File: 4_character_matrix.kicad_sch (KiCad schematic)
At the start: 26 parts, among them U25 LSHD-5503, U26 LSHD-5503, U27 LSHD-5503, U28 LSHD-5503, U29 SN74LVC244A, U30 SN74LVC244A

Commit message: change in display module
- Created new sheets
- Reordered the sheets
- Created the footprint for the display
- 3D model of the display
- MCU selection
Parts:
- removed C18, C20: 10u, symbol Device:C
- removed U25, U26, U27, U28: LSHD-5503, symbol precision_clock:LSHD-5503
- added U22, U24, U25, U27: SC10-21SURKWA, precision_clock:SC10-21SURKWA, symbol precision_clock:SC10-21SURKWA
- U23: renamed from U29; footprint (none) -> Package_SO:TSSOP-20_4.4x6.5mm_P0.65mm
- U26: renamed from U30; footprint (none) -> Package_SO:TSSOP-20_4.4x6.5mm_P0.65mm
- renumbered C19 to C7, C21 to C8, D2 to D1, D3 to D2, D4 to D3, D5 to D4, R34 to R25, R35 to R26, R36 to R27, R37 to R28, R38 to R29, R39 to R30, R40 to R31, R41 to R32, R42 to R33, R43 to R34, R44 to R35, R45 to R36
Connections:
- net BA0: now also U22.7 (A), U24.7 (A), U25.7 (A), U27.7 (A)
- net BA1: now also U22.6 (B), U24.6 (B), U25.6 (B), U27.6 (B)
- net BA2: now also U22.4 (C), U24.4 (C), U25.4 (C), U27.4 (C)
- net BA3: now also U22.2 (D), U24.2 (D), U25.2 (D), U27.2 (D)
- net BA4: now also U22.1 (E), U24.1 (E), U25.1 (E), U27.1 (E)
- net BA5: now also U22.9 (F), U24.9 (F), U25.9 (F), U27.9 (F)
- net BA6: now also U22.10 (G), U24.10 (G), U25.10 (G), U27.10 (G)
- net BA7: now also U22.5 (DP), U24.5 (DP), U25.5 (DP), U27.5 (DP)
- net BK0: now also U22.3 (CC), U22.8 (CC)
- net BK1: now also U24.3 (CC), U24.8 (CC)
- net BK2: now also U25.3 (CC), U25.8 (CC)
- net BK3: now also U27.3 (CC), U27.8 (CC)

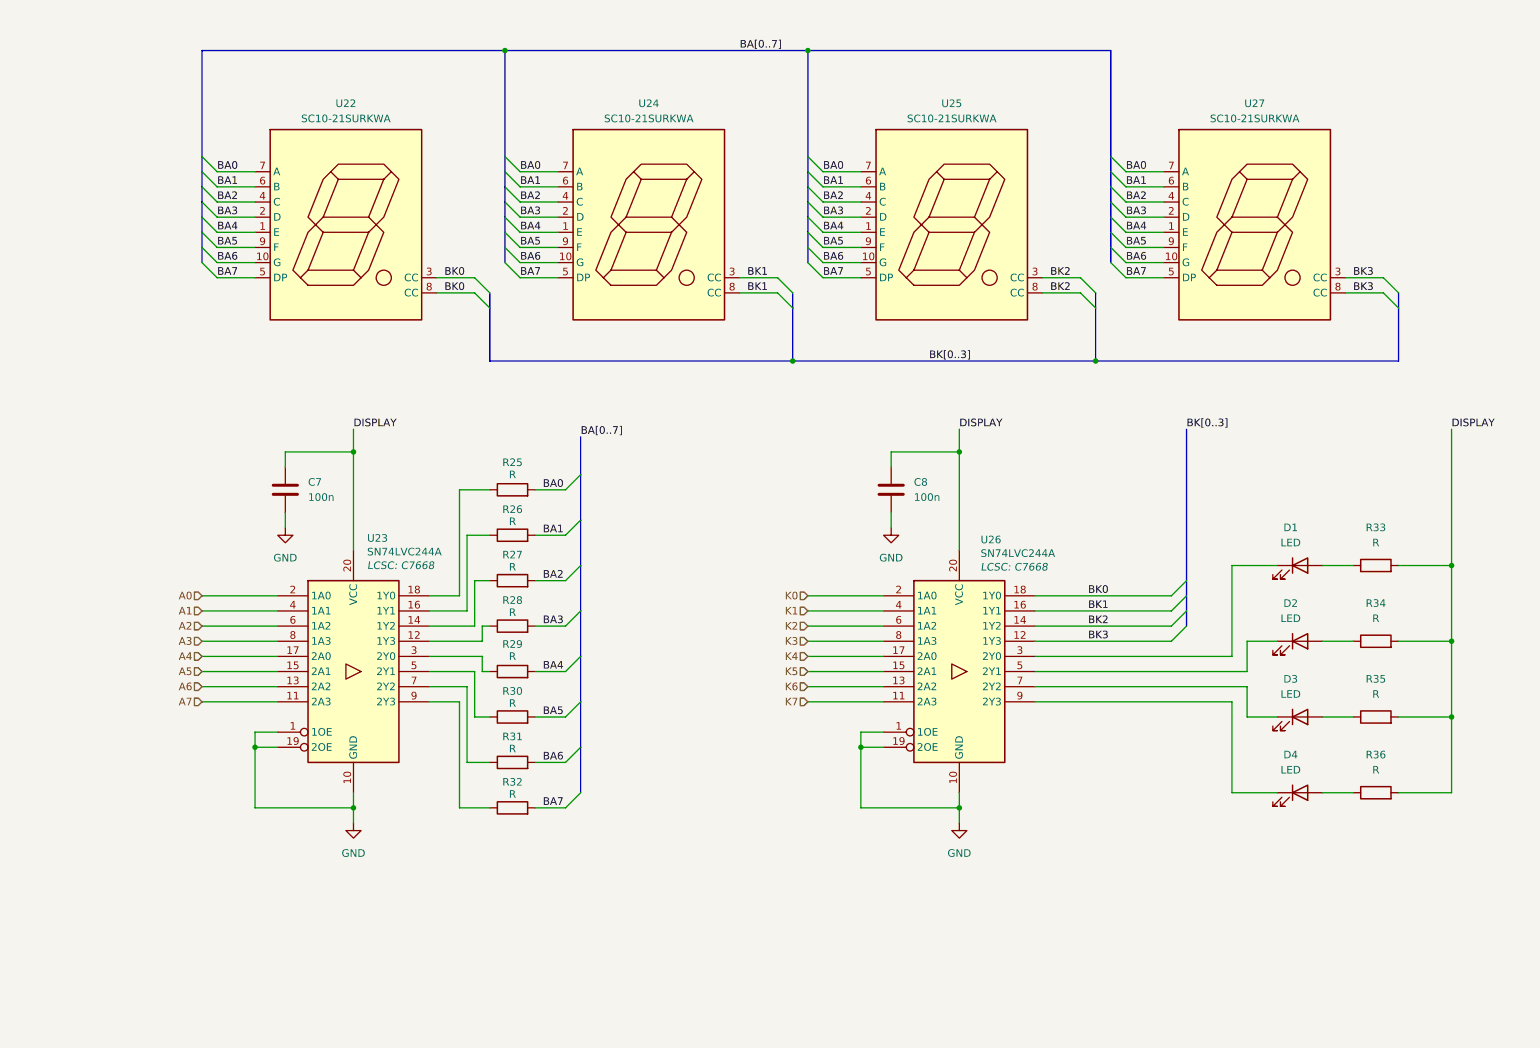
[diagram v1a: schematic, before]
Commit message: change in display module
- changes the display to a common anode type display
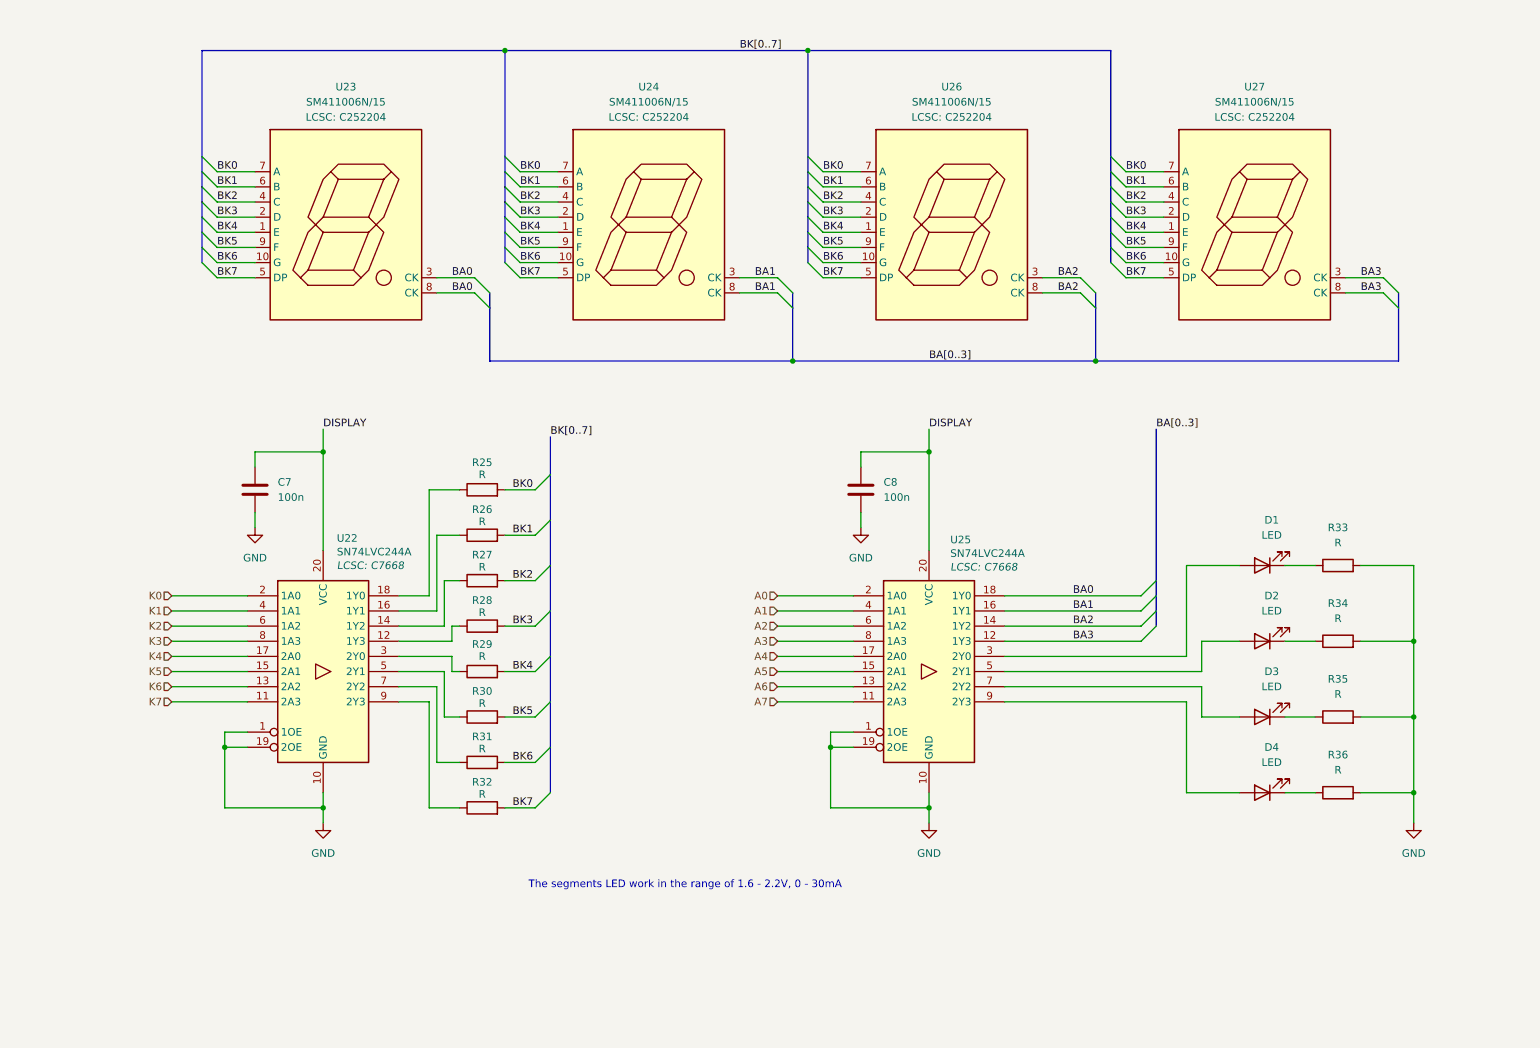
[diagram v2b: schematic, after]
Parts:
- removed U22, U24, U25, U27: SC10-21SURKWA, precision_clock:SC10-21SURKWA, symbol precision_clock:SC10-21SURKWA
- removed U23, U26: SN74LVC244A, Package_SO:TSSOP-20_4.4x6.5mm_P0.65mm, symbol 74xx:74AHC244
- added U22, U25: SN74LVC244A, Package_SO:TSSOP-20_4.4x6.5mm_P0.65mm, symbol 74xx:74AHC244
- added U23, U24, U26, U27: SM411006N/15, precision_clock:SM411006N15, symbol precision_clock:SM411006N/15
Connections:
- net A0: now also U25.2 (1A0)
- net A1: now also U25.4 (1A1)
- net A2: now also U25.6 (1A2)
- net A3: now also U25.8 (1A3)
- net A4: now also U25.17 (2A0)
- net A5: now also U25.15 (2A1)
- net A6: now also U25.13 (2A2)
- net A7: now also U25.11 (2A3)
- net BA0: now also U23.3 (CK), U23.8 (CK), U25.18 (1Y0); no longer R25.2
- net BA1: now also U24.3 (CK), U24.8 (CK), U25.16 (1Y1); no longer R26.2
- net BA2: now also U25.14 (1Y2), U26.3 (CK), U26.8 (CK); no longer R27.2
- net BA3: now also U25.12 (1Y3), U27.3 (CK), U27.8 (CK); no longer R28.2
- net BK0: now also R25.2, U23.7 (A), U24.7 (A), U26.7 (A), U27.7 (A)
- net BK1: now also R26.2, U23.6 (B), U24.6 (B), U26.6 (B), U27.6 (B)
- net BK2: now also R27.2, U23.4 (C), U24.4 (C), U26.4 (C), U27.4 (C)
- net BK3: now also R28.2, U23.2 (D), U24.2 (D), U26.2 (D), U27.2 (D)
- net DISPLAY: now also U22.20 (VCC), U25.20 (VCC); no longer R33.2, R34.2, R35.2, R36.2
- net GND: now also R33.2, R34.2, R35.2, R36.2, U22.1 (1OE), U22.10 (GND), U22.19 (2OE), U25.1 (1OE), U25.10 (GND), U25.19 (2OE)
- net K0: now also U22.2 (1A0)
- net K1: now also U22.4 (1A1)
- net K2: now also U22.6 (1A2)
- net K3: now also U22.8 (1A3)
- net K4: now also U22.17 (2A0)
- net K5: now also U22.15 (2A1)
- net K6: now also U22.13 (2A2)
- net K7: now also U22.11 (2A3)
- net at R32.1: now also U22.9 (2Y3)
- net at D1.1 (K): now also R33.1
- net at D1.2 (A): now also U25.3 (2Y0); no longer R33.1
- net at D2.1 (K): now also R34.1
- net at D3.1 (K): now also R35.1
- net at D4.1 (K): now also R36.1
- net at R29.1: now also U22.3 (2Y0)
- net at D2.2 (A): now also U25.5 (2Y1); no longer R34.1
- net at D3.2 (A): now also U25.7 (2Y2); no longer R35.1
- net at R26.1: now also U22.16 (1Y1)
- net at R30.1: now also U22.5 (2Y1)
- net at R28.1: now also U22.12 (1Y3)
- net at R27.1: now also U22.14 (1Y2)
- net at R25.1: now also U22.18 (1Y0)
- net at R31.1: now also U22.7 (2Y2)
- net at D4.2 (A): now also U25.9 (2Y3); no longer R36.1
- net BA4 renamed BK4
- net BK4: now also U23.1 (E), U24.1 (E), U26.1 (E), U27.1 (E)
- net BA5 renamed BK5
- net BK5: now also U23.9 (F), U24.9 (F), U26.9 (F), U27.9 (F)
- net BA6 renamed BK6
- net BK6: now also U23.10 (G), U24.10 (G), U26.10 (G), U27.10 (G)
- net BA7 renamed BK7
- net BK7: now also U23.5 (DP), U24.5 (DP), U26.5 (DP), U27.5 (DP)
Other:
- note added: "The segments LED work in the range of 1.6 - 2.2V, 0 - 30mA"

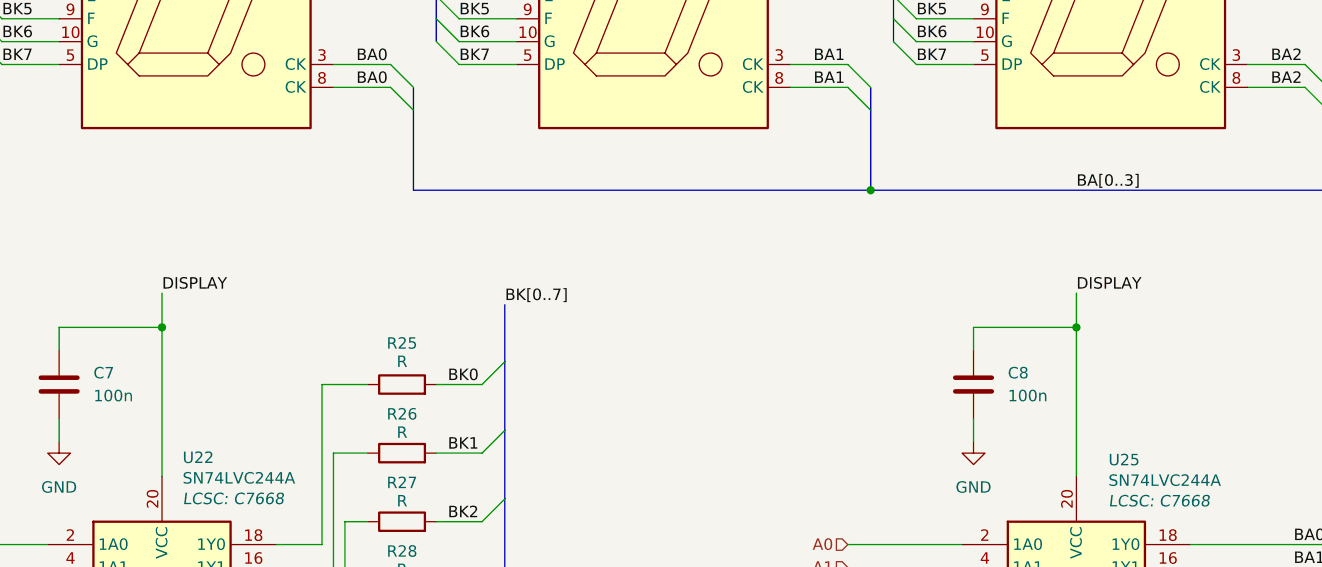
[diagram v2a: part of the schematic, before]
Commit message: primary MCU changes
- added preliminary decoupling
- added LSE
- added flash memory
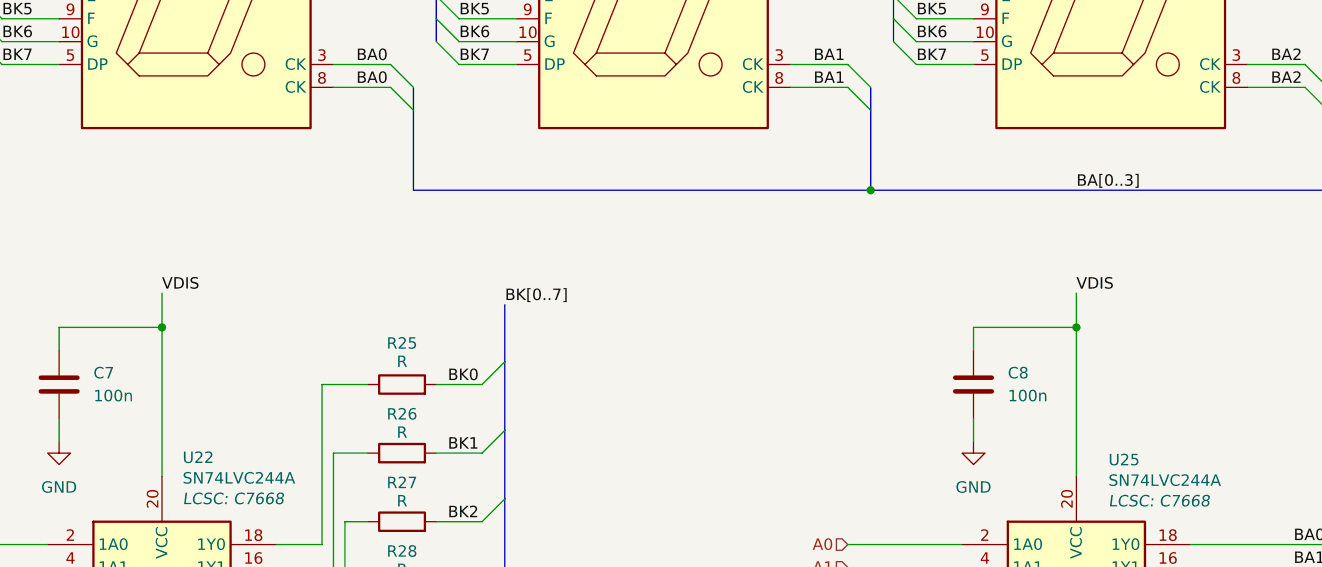
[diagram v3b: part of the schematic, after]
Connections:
- net DISPLAY renamed VDIS
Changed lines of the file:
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@@
 		)
 	)
-	(label "DISPLAY"
+	(label "VDIS"
 		(at 71.12 88.9 0)
 		(effects
@@
 		)
 	)
-	(label "DISPLAY"
+	(label "VDIS"
 		(at 172.72 88.9 0)
 		(effects

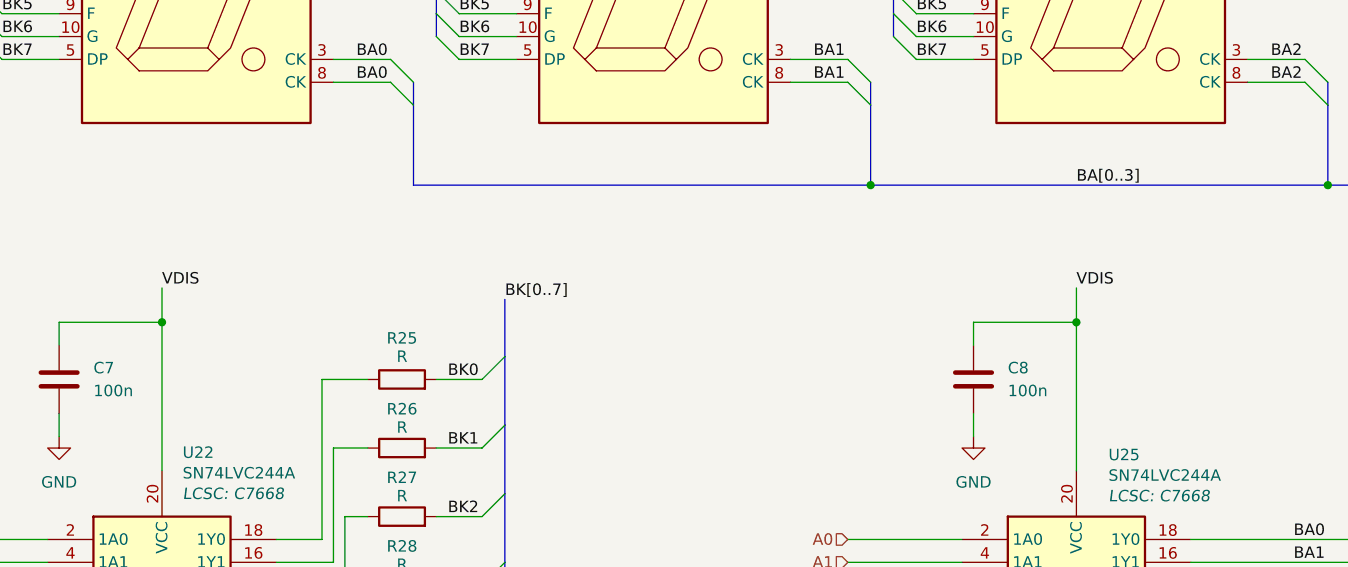
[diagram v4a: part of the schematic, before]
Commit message: minor changes
- removed the power, ambient light sensing circuits.
- minor changes in the primary MCU pinout.
- USB connector moved to MCU sheet.
- ESD protection added.
- removed the test points from the individual sheets.
- Improved readability.
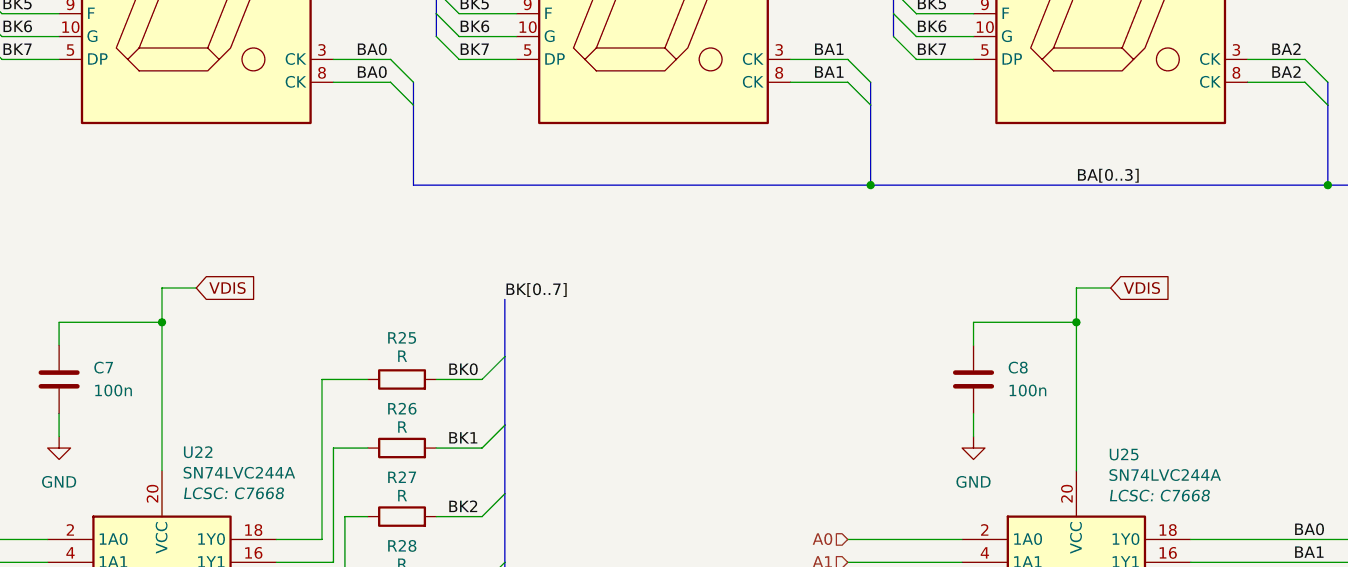
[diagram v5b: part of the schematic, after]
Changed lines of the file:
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@@
+	)
+	(junction
+		(at 71.12 92.71)
+		(diameter 0)
+		(color 0 0 0 0)
+	)
+	(junction
+		(at 172.72 92.71)
+		(diameter 0)
+		(color 0 0 0 0)
 	)
 	(junction
@@
 	)
 	(junction
-		(at 71.12 92.71)
-		(diameter 0)
-		(color 0 0 0 0)
-	)
-	(junction
-		(at 172.72 92.71)
-		(diameter 0)
-		(color 0 0 0 0)
-	)
-	(junction
 		(at 254 137.16)
 		(diameter 0)
@@
 		)
 	)
+	(wire
+		(pts
+			(xy 176.53 88.9) (xy 172.72 88.9)
+		)
+		(stroke
+			(width 0)
+			(type default)
+		)
+	)
 	(bus
 		(pts
@@
 	(wire
 		(pts
+			(xy 71.12 88.9) (xy 71.12 92.71)
+		)
+		(stroke
+			(width 0)
+			(type default)
+		)
+	)
+	(wire
+		(pts
 			(xy 54.61 142.24) (xy 58.42 142.24)
 		)
@@
 	(wire
 		(pts
+			(xy 74.93 88.9) (xy 71.12 88.9)
+		)
+		(stroke
+			(width 0)
+			(type default)
+		)
+	)
+	(wire
+		(pts
 			(xy 245.11 137.16) (xy 254 137.16)
 		)
@@
 	(wire
 		(pts
+			(xy 172.72 88.9) (xy 172.72 92.71)
+		)
+		(stroke
+			(width 0)
+			(type default)
+		)
+	)
+	(wire
+		(pts
 			(xy 53.34 58.42) (xy 59.69 58.42)
 		)
@@
 		)
 	)
-	(wire
-		(pts
-			(xy 172.72 88.9) (xy 172.72 92.71)
-		)
-		(stroke
-			(width 0)
-			(type default)
-		)
-	)
 	(bus
 		(pts
@@
 		(pts
 			(xy 83.82 134.62) (xy 88.9 134.62)
-		)
-		(stroke
-			(width 0)
-			(type default)
-		)
-	)
-	(wire
-		(pts
-			(xy 71.12 88.9) (xy 71.12 92.71)
 		)
 		(stroke
@@
 		)
 	)
-	(label "VDIS"
-		(at 71.12 88.9 0)
-		(effects
-			(font
-				(size 1.27 1.27)
-			)
-			(justify left bottom)
-		)
-	)
 	(label "BK3"
 		(at 53.34 53.34 0)
@@
 		)
 	)
-	(label "VDIS"
-		(at 172.72 88.9 0)
-		(effects
-			(font
-				(size 1.27 1.27)
-			)
-			(justify left bottom)
-		)
-	)
 	(label "BA3"
 		(at 245.11 66.04 0)
@@
 		)
 	)
+	(global_label "VDIS"
+		(shape input)
+		(at 176.53 88.9 0)
+		(fields_autoplaced yes)
+		(effects
+			(font
+				(size 1.27 1.27)
+			)
+			(justify left)
+		)
+		(property "Intersheetrefs" "${INTERSHEET_REFS}"
+			(at 183.6881 88.9 0)
+			(effects
+				(font
+					(size 1.27 1.27)
+				)
+				(justify left)
+				(hide yes)
+			)
+		)
+	)
+	(global_label "VDIS"
+		(shape input)
+		(at 74.93 88.9 0)
+		(fields_autoplaced yes)
+		(effects
+			(font
+				(size 1.27 1.27)
+			)
+			(justify left)
+		)
+		(property "Intersheetrefs" "${INTERSHEET_REFS}"
+			(at 82.0881 88.9 0)
+			(effects
+				(font
+					(size 1.27 1.27)
+				)
+				(justify left)
+				(hide yes)
+			)
+		)
+	)
